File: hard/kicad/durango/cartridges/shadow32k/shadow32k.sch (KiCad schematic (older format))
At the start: 12 parts, among them J1 to Computer, J2 SD Interface, U1 27/28C256, U2 62256, U4 74HC174, U5 74HC139, U6 74HC245, U7 74HC139

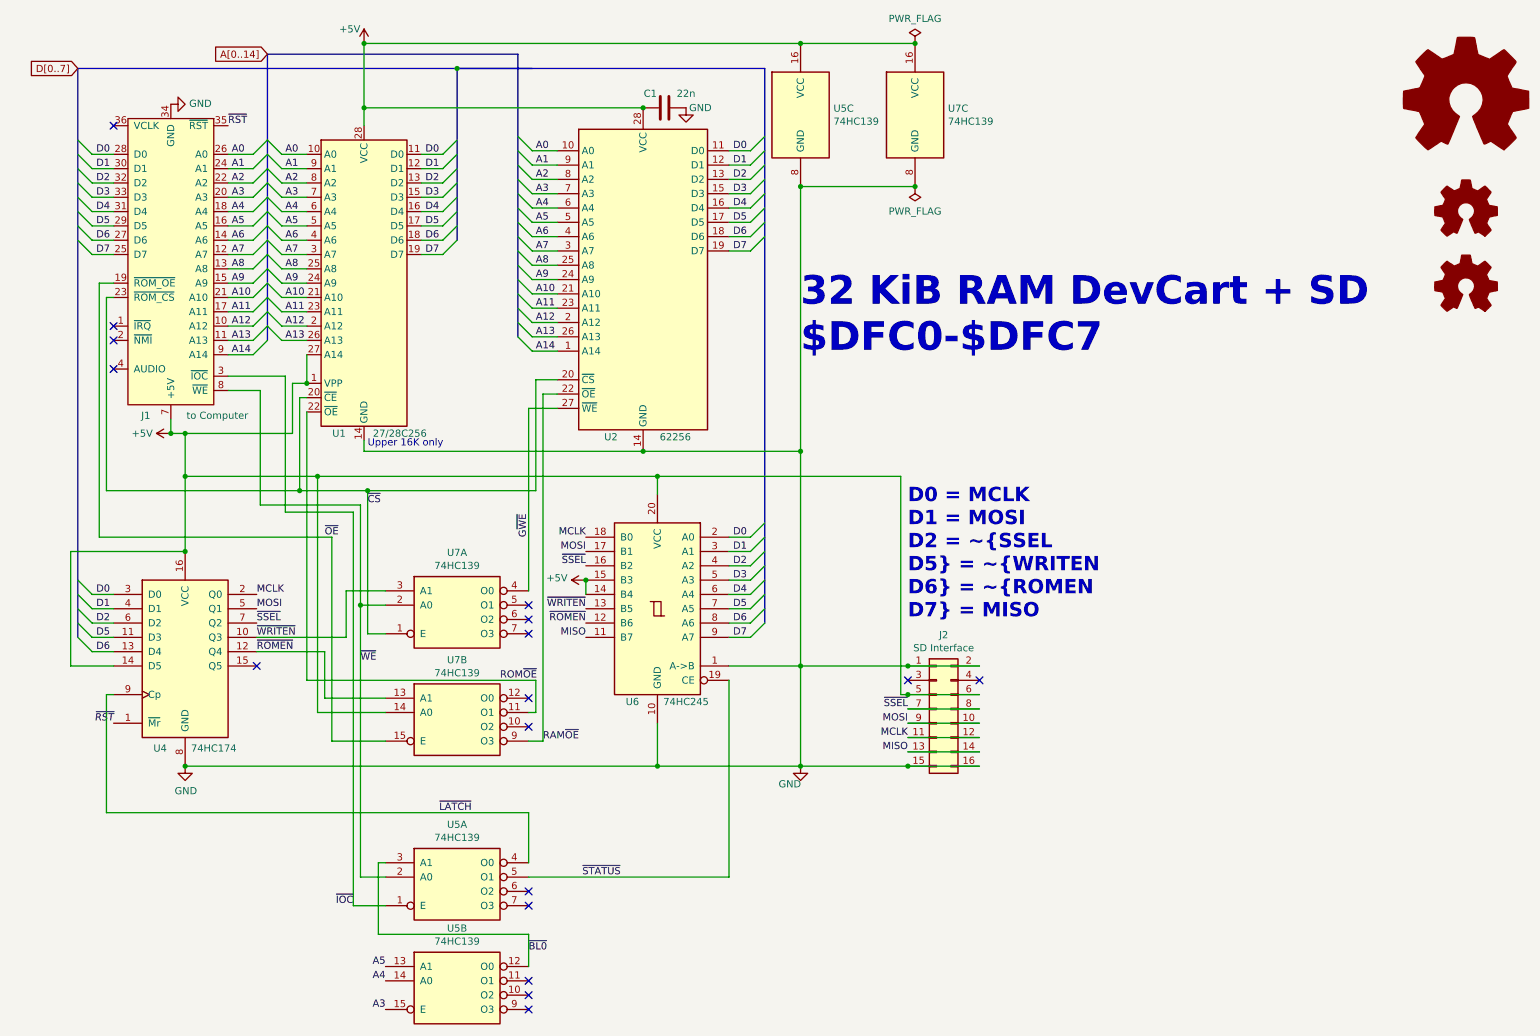
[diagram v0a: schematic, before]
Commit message: alternative routing in ShadowRAM
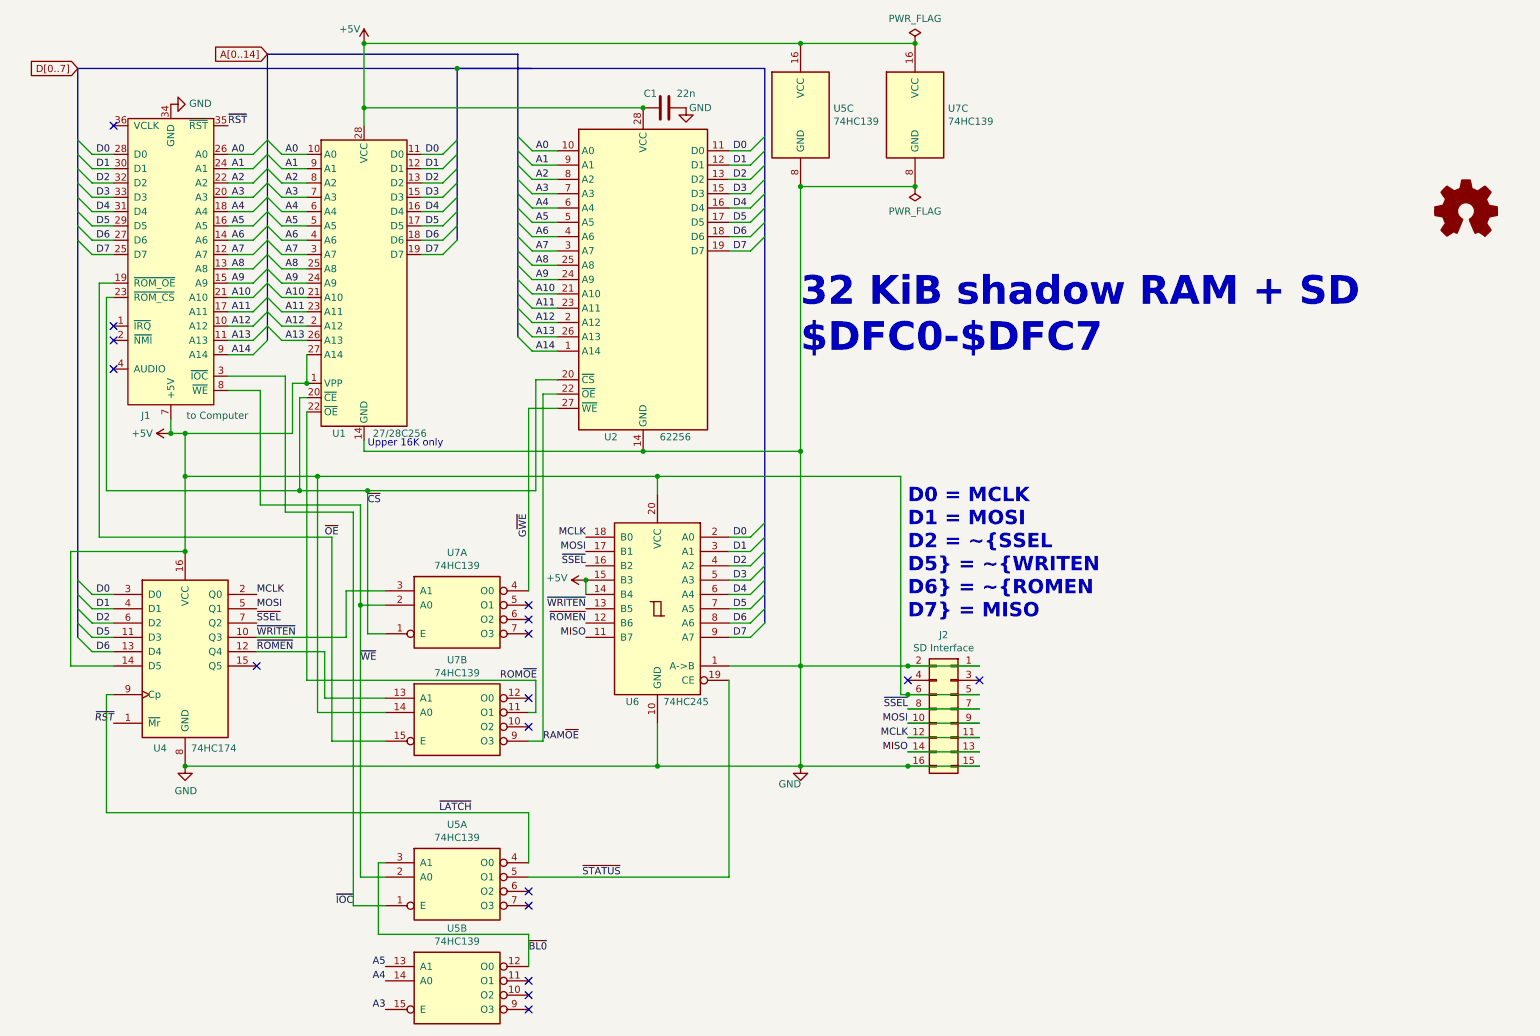
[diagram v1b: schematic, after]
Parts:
- removed LOGO1: Logo_Open_Hardware_Large, Symbol:OSHW-Logo2_24.3x20mm_SilkScreen, symbol Graphic:Logo_Open_Hardware_Large
- removed LOGO3: Logo_Open_Hardware_Small, durango:durango-x90, symbol Graphic:Logo_Open_Hardware_Small
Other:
- note added: "32 KiB shadow RAM + SD\n$DFC0-$DFC7"
- note removed: "32 KiB RAM DevCart + SD\n$DFC0-$DFC7"
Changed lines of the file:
@@
 L Connector_Generic:Conn_02x08_Odd_Even J2
 U 1 1 63B847A5
-P 6900 5350
-F 0 "J2" H 6950 5867 50  0000 C CNN
-F 1 "SD Interface" H 6950 5776 50  0000 C CNN
-F 2 "Connector_PinHeader_2.54mm:PinHeader_2x08_P2.54mm_Horizontal" H 6900 5350 50  0001 C CNN
-F 3 "~" H 6900 5350 50  0001 C CNN
-	1    6900 5350
-	1    0    0    -1
+P 7000 5350
+F 0 "J2" H 7050 5867 50  0000 C CNN
+F 1 "SD Interface" H 7050 5776 50  0000 C CNN
+F 2 "Connector_PinHeader_2.54mm:PinHeader_2x08_P2.54mm_Horizontal" H 7000 5350 50  0001 C CNN
+F 3 "~" H 7000 5350 50  0001 C CNN
+	1    7000 5350
+	-1   0    0    -1
 $EndComp
 Wire Wire Line
@@
 Connection ~ 6700 5750
 $Comp
-L Graphic:Logo_Open_Hardware_Large LOGO1
-U 1 1 63BF327C
-P 10600 1100
-F 0 "LOGO1" H 10600 1600 50  0001 C CNN
-F 1 "Logo_Open_Hardware_Large" H 10600 700 50  0001 C CNN
-F 2 "Symbol:OSHW-Logo2_24.3x20mm_SilkScreen" H 10600 1100 50  0001 C CNN
-F 3 "~" H 10600 1100 50  0001 C CNN
-	1    10600 1100
-	1    0    0    -1
-$EndComp
-$Comp
 L Graphic:Logo_Open_Hardware_Small LOGO2
 U 1 1 63BF61E9
@@
 Text Label 4050 4150 1    50   ~ 0
 G~WE
-$Comp
-L Graphic:Logo_Open_Hardware_Small LOGO3
-U 1 1 63C2970C
-P 10600 2400
-F 0 "LOGO3" H 10600 2675 50  0001 C CNN
-F 1 "Logo_Open_Hardware_Small" H 10600 2175 50  0001 C CNN
-F 2 "durango:durango-x90" H 10600 2400 50  0001 C CNN
-F 3 "~" H 10600 2400 50  0001 C CNN
-	1    10600 2400
-	1    0    0    -1
-$EndComp
 NoConn ~ 4050 6625
 Wire Wire Line
@@
 ~BL0
 Text Notes 5950 2875 0    200  ~ 40
-32 KiB RAM DevCart + SD\n$DFC0-$DFC7
+32 KiB shadow RAM + SD\n$DFC0-$DFC7
 Text Notes 6700 4725 0    100  ~ 20
 D0 = MCLK\nD1 = MOSI\nD2 = ~SSEL\nD5 = ~WRITEN\nD6 = ~ROMEN\nD7 = MISO

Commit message: 32KiB enabled ShadowRAM
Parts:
- added JP1: 32KiB, Jumper:SolderJumper-3_P1.3mm_Bridged12_RoundedPad1.0x1.5mm, symbol Jumper:SolderJumper_3_Bridged12
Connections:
- net +5V: now also JP1.1 (A); no longer U1.1 (VPP), U1.27 (A14)
- net A14: now also U1.1 (VPP), JP1.3 (B)
- new net MA14: JP1.2 (C), U1.27 (A14)
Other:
- note added: "Set this for\n27C256 only"
- note removed: "Upper 16K only"
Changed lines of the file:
@@
 Sheet 1 1
 Title "Compact 32 KiB Shadow RAM cartridge for Durango-X"
-Date "2023-10-22"
-Rev "v1"
+Date "2023-10-24"
+Rev "v1.1"
 Comp "@zuiko21"
 Comment1 ""
@@
 	2450 3825 2925 3825
 Wire Wire Line
-	2500 2875 2500 3075
-Wire Wire Line
 	1550 3425 1650 3425
-Wire Wire Line
-	2400 3425 2400 3075
-Wire Wire Line
-	2400 3075 2500 3075
 Connection ~ 1550 3425
-Connection ~ 2500 3075
-Text Notes 2925 3525 0    50   ~ 0
-Upper 16K only
 Text Label 1950 1275 0    50   ~ 0
 ~RST
@@
 Wire Wire Line
 	1650 4250 1650 3725
-Connection ~ 1650 3425
-Wire Wire Line
-	1650 3425 2400 3425
 Wire Wire Line
 	1150 4550 1000 4550
@@
 Connection ~ 1650 5750
 Wire Wire Line
-	1950 3025 2350 3025
-Wire Wire Line
-	2350 3025 2350 3975
+	1950 3025 2200 3025
 Text Label 2825 6725 2    50   ~ 0
 ~IOC
@@
 ~STATUS
 Wire Wire Line
-	2350 3975 2825 3975
+	2200 3975 2825 3975
 $Comp
 L 74xx:74LS139 U5
@@
 Wire Wire Line
 	2825 3975 2825 6725
+Wire Wire Line
+	2200 3025 2200 3975
+Wire Wire Line
+	2325 3075 2400 3075
+Text Label 2475 3075 2    50   ~ 0
+A14
+Entry Wire Line
+	2325 3075 2225 2975
+Text Label 2500 2875 2    50   ~ 0
+MA14
+$Comp
+L Jumper:SolderJumper_3_Bridged12 JP1
+U 1 1 653E313B
+P 3550 2875
+F 0 "JP1" V 3504 2943 50  0000 L CNN
+F 1 "32KiB" V 3595 2943 50  0000 L CNN
+F 2 "Jumper:SolderJumper-3_P1.3mm_Bridged12_RoundedPad1.0x1.5mm" H 3550 2875 50  0001 C CNN
+F 3 "~" H 3550 2875 50  0001 C CNN
+	1    3550 2875
+	0    1    1    0
+$EndComp
+Wire Wire Line
+	2400 3075 2400 3600
+Wire Wire Line
+	2400 3600 3550 3600
+Wire Wire Line
+	3550 3600 3550 3075
+Connection ~ 2400 3075
+Wire Wire Line
+	2400 3075 2500 3075
+Wire Wire Line
+	3400 2875 2500 2875
 Wire Bus Line
 	3550 875  3550 2075
-Wire Bus Line
-	2225 775  2225 2775
 Wire Bus Line
 	900  875  900  4850
@@
 	3975 775  3975 2750
 Wire Bus Line
+	2225 775  2225 2975
+Wire Bus Line
 	5700 875  5700 4750
+$Comp
+L power:+5V #PWR0108
+U 1 1 653FB2FC
+P 3550 2675
+F 0 "#PWR0108" H 3550 2525 50  0001 C CNN
+F 1 "+5V" H 3565 2848 50  0000 C CNN
+F 2 "" H 3550 2675 50  0001 C CNN
+F 3 "" H 3550 2675 50  0001 C CNN
+	1    3550 2675
+	1    0    0    -1
+$EndComp
+Text Notes 3575 3200 0    50   ~ 0
+Set this for\n27C256 only
 $EndSCHEMATC
